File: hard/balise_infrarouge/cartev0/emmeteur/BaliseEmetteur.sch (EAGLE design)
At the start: 58 parts, among them IC1 MEGA8-AI, IC2 74AHC1G02DBV, IC3 7812TV, Q1 16MHz, T1 2SC1307

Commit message: carte emmeteur finale ?
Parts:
- removed R3, R4: 10k, rcl:R-EU_0207/2V
- added C12, C13, C3, C5, C8, C9: 100n, rcl:C-EUC0805
- added JP2: (no value), SparkFun-Connectors:ARDUINO_SERIAL_PROGRAMPTH
- added R14: 4k, adafruit:R-US_M0805
- added R15: 10k, adafruit:R-US_M0805
- JP1: value (none) -> AVR_SPI_PRG_62X3_LOCK; device pinhead:PINHD-2X3 -> SparkFun-Connectors:AVR_SPI_PRG_62X3_LOCK
- Q1: device crystal:CRYSTALHC49UP -> adafruit:CRYSTALHC49S
- R10, R12, R6, R7, R8, R9: device rcl:R-EU_0207/2V -> adafruit:R-US_M0805
- R13, R2: device adafruit:R-US_R0805W -> adafruit:R-US_M0805
- R5: value 4k -> 10k; device rcl:R-EU_0207/2V -> adafruit:R-US_M0805
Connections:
- removed net N$19: BATTERY_18V-1.KL, C2.1, IC3.VI
- new net +18V: BATTERY_18V-1.KL, C2.1, IC3.VI, R15.2
- new net TX_SOFT: IC1.PB1(OC1A), IC2A.I0
- new net UART_RX: IC1.PD0(RXD), JP2.TXO
- net +12V: no longer R3.2
- net +5V: now also JP2.VCC
- net BATT_ADC: now also R15.1, R5.2; no longer R3.1, R4.2
- net GND: now also C12.2, C13.2, C3.2, C5.2, C8.2, C9.2, JP2.GND, R5.1; no longer R4.1
- net N$15: now also R14.1; no longer R5.1
- net N$23: now also C3.1
- net N$27: now also C5.1
- net N$29: now also C8.1
- net N$3: now also R14.2; no longer R5.2
- net N$30: now also C9.1
- net N$32: now also C12.1
- net N$33: now also C13.1
- net PWM: now also IC1.PD7(AIN1); no longer IC1.PB1(OC1A)
- net UART_TX: now also JP2.RXI; no longer IC2A.I0

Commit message: maj emetteur + fini recepteur part 1
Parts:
- renumbered JP2 to FTDI_ARDUINO
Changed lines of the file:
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@@
 <part name="R2" library="adafruit" deviceset="R-US_" device="M0805" value="1k"/>
 <part name="V14" library="supply3" deviceset="+5V" device=""/>
-<part name="JP2" library="SparkFun-Connectors" deviceset="ARDUINO_SERIAL_PROGRAM" device="PTH"/>
+<part name="FTDI_ARDUINO" library="SparkFun-Connectors" deviceset="ARDUINO_SERIAL_PROGRAM" device="PTH"/>
 <part name="V15" library="supply3" deviceset="+5V" device=""/>
 <part name="GND10" library="supply3" deviceset="GND" device=""/>
@@
 <instance part="R2" gate="G$1" x="99.06" y="111.76" rot="R180"/>
 <instance part="V14" gate="+5V" x="76.2" y="114.3"/>
-<instance part="JP2" gate="G$1" x="238.76" y="81.28" rot="R180"/>
+<instance part="FTDI_ARDUINO" gate="G$1" x="238.76" y="81.28" rot="R180"/>
 <instance part="V15" gate="+5V" x="226.06" y="78.74" rot="R90"/>
 <instance part="GND10" gate="1" x="223.52" y="73.66" rot="R270"/>
@@
 </segment>
 <segment>
-<pinref part="JP2" gate="G$1" pin="GND"/>
+<pinref part="FTDI_ARDUINO" gate="G$1" pin="GND"/>
 <pinref part="GND10" gate="1" pin="GND"/>
 <wire x1="226.06" y1="73.66" x2="233.68" y2="73.66" width="0.1524" layer="91"/>
@@
 </segment>
 <segment>
-<pinref part="JP2" gate="G$1" pin="VCC"/>
+<pinref part="FTDI_ARDUINO" gate="G$1" pin="VCC"/>
 <pinref part="V15" gate="+5V" pin="+5V"/>
 <wire x1="228.6" y1="78.74" x2="233.68" y2="78.74" width="0.1524" layer="91"/>
@@
 <wire x1="233.68" y1="83.82" x2="220.98" y2="83.82" width="0.1524" layer="91"/>
 <label x="218.44" y="83.82" size="1.778" layer="95"/>
-<pinref part="JP2" gate="G$1" pin="RXI"/>
+<pinref part="FTDI_ARDUINO" gate="G$1" pin="RXI"/>
 <junction x="233.68" y="83.82"/>
 </segment>
@@
 </segment>
 <segment>
-<pinref part="JP2" gate="G$1" pin="TXO"/>
+<pinref part="FTDI_ARDUINO" gate="G$1" pin="TXO"/>
 <wire x1="233.68" y1="81.28" x2="220.98" y2="81.28" width="0.1524" layer="91"/>
 <label x="218.44" y="81.28" size="1.778" layer="95"/>

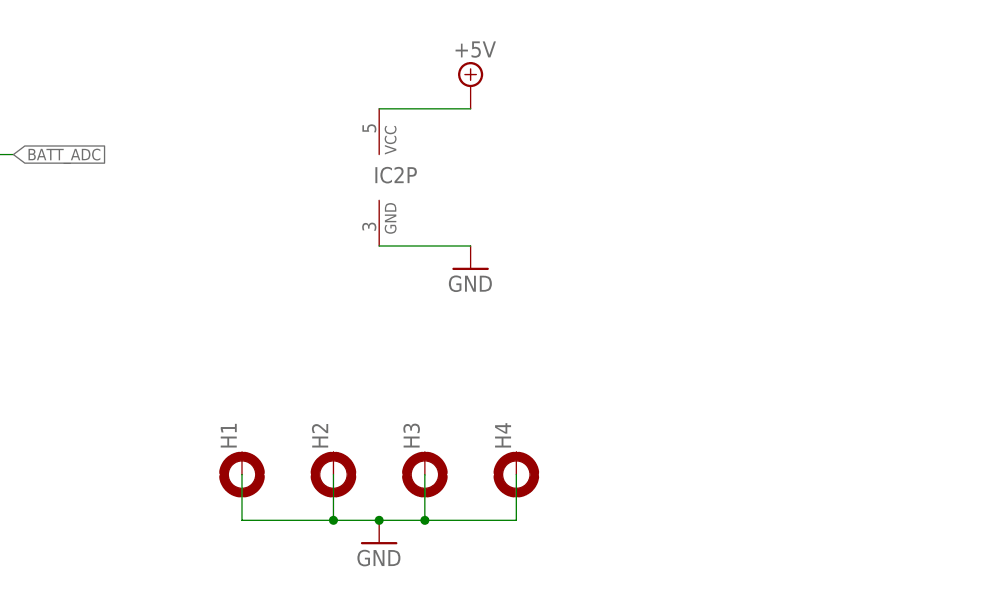
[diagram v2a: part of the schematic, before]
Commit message: maj carte extension nucleo
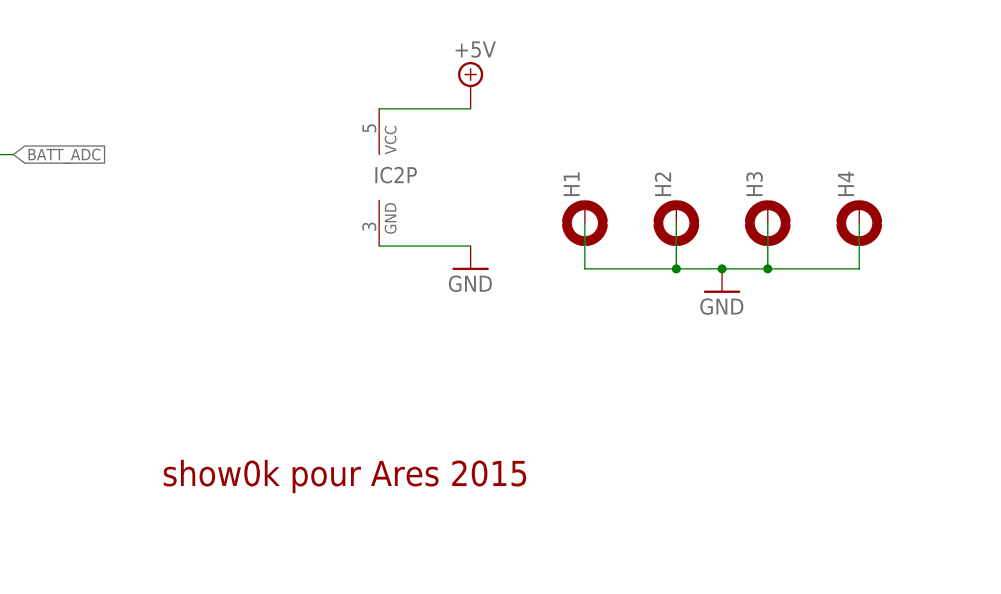
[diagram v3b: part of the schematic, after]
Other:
- note added: "show0k pour Ares 2015"
- moved on the sheet: H1, H2, H3, H4
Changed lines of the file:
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@@
 <layer number="56" name="wert" color="7" fill="1" visible="no" active="no"/>
 <layer number="57" name="tCAD" color="7" fill="1" visible="no" active="no"/>
+<layer number="59" name="tCarbon" color="7" fill="1" visible="no" active="no"/>
+<layer number="60" name="bCarbon" color="7" fill="1" visible="no" active="no"/>
 <layer number="91" name="Nets" color="2" fill="1" visible="yes" active="yes"/>
 <layer number="92" name="Busses" color="1" fill="1" visible="yes" active="yes"/>
@@
 <layer number="127" name="_tValues" color="7" fill="1" visible="yes" active="yes"/>
 <layer number="128" name="_bValues" color="7" fill="1" visible="yes" active="yes"/>
+<layer number="129" name="Mask" color="7" fill="1" visible="yes" active="yes"/>
 <layer number="131" name="tAdjust" color="7" fill="1" visible="no" active="yes"/>
 <layer number="132" name="bAdjust" color="7" fill="1" visible="no" active="yes"/>
@@
 <part name="LED23" library="led" deviceset="LED" device="B155"/>
 <part name="LED24" library="led" deviceset="LED" device="B155"/>
-<part name="FRAME2" library="frames" deviceset="A4L-LOC" device=""/>
+<part name="TEST" library="frames" deviceset="A4L-LOC" device=""/>
 <part name="BATTERY_18V" library="con-ptr500" deviceset="AK500/2" device="" value="ALIM"/>
 <part name="V4" library="supply2" deviceset="+12V" device=""/>
@@
 <text x="10.16" y="17.78" size="1.778" layer="91">Attention : le montage est fait pour fonctionner en pulse</text>
 <text x="10.16" y="10.16" size="1.778" layer="91">Une activation continue du transistor peut cramer les leds d'émission</text>
+<text x="163.83" y="13.97" size="2.794" layer="94" font="vector" ratio="14">show0k pour Ares 2015</text>
 </plain>
 <instances>
-<instance part="H1" gate="G$1" x="172.72" y="15.24" rot="R90"/>
-<instance part="H2" gate="G$1" x="182.88" y="15.24" rot="R90"/>
-<instance part="H3" gate="G$1" x="193.04" y="15.24" rot="R90"/>
-<instance part="H4" gate="G$1" x="203.2" y="15.24" rot="R90"/>
-<instance part="GND2" gate="1" x="187.96" y="7.62"/>
+<instance part="H1" gate="G$1" x="210.82" y="43.18" rot="R90"/>
+<instance part="H2" gate="G$1" x="220.98" y="43.18" rot="R90"/>
+<instance part="H3" gate="G$1" x="231.14" y="43.18" rot="R90"/>
+<instance part="H4" gate="G$1" x="241.3" y="43.18" rot="R90"/>
+<instance part="GND2" gate="1" x="226.06" y="35.56"/>
 <instance part="V2" gate="+5V" x="30.48" y="50.8"/>
 <instance part="GND1" gate="1" x="30.48" y="38.1"/>
@@
 <instance part="LED23" gate="G$1" x="241.3" y="132.08"/>
 <instance part="LED24" gate="G$1" x="241.3" y="121.92"/>
-<instance part="FRAME2" gate="G$1" x="0" y="0"/>
+<instance part="TEST" gate="G$1" x="0" y="0"/>
 <instance part="BATTERY_18V" gate="-1" x="17.78" y="134.62"/>
 <instance part="BATTERY_18V" gate="-2" x="17.78" y="129.54"/>
@@
 <net name="GND" class="0">
 <segment>
-<wire x1="187.96" y1="10.16" x2="193.04" y2="10.16" width="0.1524" layer="91"/>
-<wire x1="193.04" y1="10.16" x2="203.2" y2="10.16" width="0.1524" layer="91"/>
-<wire x1="203.2" y1="10.16" x2="203.2" y2="15.24" width="0.1524" layer="91"/>
-<wire x1="193.04" y1="15.24" x2="193.04" y2="10.16" width="0.1524" layer="91"/>
-<wire x1="187.96" y1="10.16" x2="182.88" y2="10.16" width="0.1524" layer="91"/>
-<wire x1="182.88" y1="10.16" x2="182.88" y2="15.24" width="0.1524" layer="91"/>
-<wire x1="182.88" y1="10.16" x2="172.72" y2="10.16" width="0.1524" layer="91"/>
-<wire x1="172.72" y1="10.16" x2="172.72" y2="15.24" width="0.1524" layer="91"/>
-<junction x="193.04" y="10.16"/>
-<junction x="187.96" y="10.16"/>
-<junction x="182.88" y="10.16"/>
+<wire x1="226.06" y1="38.1" x2="231.14" y2="38.1" width="0.1524" layer="91"/>
+<wire x1="231.14" y1="38.1" x2="241.3" y2="38.1" width="0.1524" layer="91"/>
+<wire x1="241.3" y1="38.1" x2="241.3" y2="43.18" width="0.1524" layer="91"/>
+<wire x1="231.14" y1="43.18" x2="231.14" y2="38.1" width="0.1524" layer="91"/>
+<wire x1="226.06" y1="38.1" x2="220.98" y2="38.1" width="0.1524" layer="91"/>
+<wire x1="220.98" y1="38.1" x2="220.98" y2="43.18" width="0.1524" layer="91"/>
+<wire x1="220.98" y1="38.1" x2="210.82" y2="38.1" width="0.1524" layer="91"/>
+<wire x1="210.82" y1="38.1" x2="210.82" y2="43.18" width="0.1524" layer="91"/>
+<junction x="231.14" y="38.1"/>
+<junction x="226.06" y="38.1"/>
+<junction x="220.98" y="38.1"/>
 <pinref part="GND2" gate="1" pin="GND"/>
 <pinref part="H4" gate="G$1" pin="MOUNT"/>

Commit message: maj connectyeur bt + ftdi carte elettrice
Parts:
- added SV1: Bluetooth, con-lstb:MA04-1
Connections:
- net +5V: now also SV1.1
- net GND: now also SV1.2
- net UART_RX: now also SV1.3
- net UART_TX: now also SV1.4
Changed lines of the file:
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@@
 <part name="GND16" library="supply3" deviceset="GND" device=""/>
 <part name="GND17" library="supply3" deviceset="GND" device=""/>
+<part name="SV1" library="con-lstb" deviceset="MA04-1" device="" value="Bluetooth"/>
+<part name="P+10" library="supply1" deviceset="+5V" device=""/>
+<part name="GND19" library="SparkFun-Aesthetics" deviceset="GND" device=""/>
 </parts>
 <sheets>
@@
 <instance part="GND16" gate="1" x="228.6" y="111.76"/>
 <instance part="GND17" gate="1" x="251.46" y="111.76"/>
+<instance part="SV1" gate="1" x="213.36" y="76.2" rot="R180"/>
+<instance part="P+10" gate="1" x="203.2" y="86.36"/>
+<instance part="GND19" gate="1" x="193.04" y="81.28" rot="R180"/>
 </instances>
 <busses>
@@
 <pinref part="GND17" gate="1" pin="GND"/>
 <wire x1="251.46" y1="114.3" x2="248.92" y2="114.3" width="0.1524" layer="91"/>
+</segment>
+<segment>
+<pinref part="SV1" gate="1" pin="2"/>
+<wire x1="193.04" y1="78.74" x2="205.74" y2="78.74" width="0.1524" layer="91"/>
+<pinref part="GND19" gate="1" pin="GND"/>
 </segment>
 </net>
@@
 <pinref part="V15" gate="+5V" pin="+5V"/>
 <wire x1="228.6" y1="78.74" x2="233.68" y2="78.74" width="0.1524" layer="91"/>
+</segment>
+<segment>
+<pinref part="P+10" gate="1" pin="+5V"/>
+<wire x1="203.2" y1="83.82" x2="203.2" y2="81.28" width="0.1524" layer="91"/>
+<pinref part="SV1" gate="1" pin="1"/>
+<wire x1="203.2" y1="81.28" x2="205.74" y2="81.28" width="0.1524" layer="91"/>
 </segment>
 </net>
@@
 <junction x="233.68" y="83.82"/>
 </segment>
+<segment>
+<pinref part="SV1" gate="1" pin="4"/>
+<wire x1="195.58" y1="73.66" x2="205.74" y2="73.66" width="0.1524" layer="91"/>
+<label x="193.04" y="73.66" size="1.778" layer="95"/>
+</segment>
 </net>
 <net name="ISP_MOSI" class="0">
@@
 <label x="218.44" y="81.28" size="1.778" layer="95"/>
 </segment>
-</net>
+<segment>
+<pinref part="SV1" gate="1" pin="3"/>
+<wire x1="195.58" y1="76.2" x2="205.74" y2="76.2" width="0.1524" layer="91"/>
+<label x="193.04" y="76.2" size="1.778" layer="95"/>
+</segment>
+</net>
